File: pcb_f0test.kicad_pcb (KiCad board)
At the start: 2 copper layers, 50 x 6 mm, 36 parts, among them P1 CONN_02X04, P2 CONN_01X02, U1 STM32F042GxU, U2 LP2985LV

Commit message: Fairly good routing now.
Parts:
- moved C2 0.20 mm to (43.1, 63.2)
- moved C4 0.20 mm to (44.1, 63.2)
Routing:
- net /boot0: track 21.3 -> 25.5 mm
- net /ldr6: track 32.0 -> 31.1 mm
- net /ldb1: track 32.8 -> 32.0 mm
- net /ldr2: track 13.3 -> 14.0 mm
- net /ldr5: track 28.5 -> 27.8 mm
- net +3V3: track 56.4 -> 55.8 mm
- added copper zone on B.Cu, net +3V3

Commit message: Some misc. changes.
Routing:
- added copper zone on F.Cu, net +3V3
- added copper zone on B.Cu, net GND
- added copper zone on F.Cu, net GND

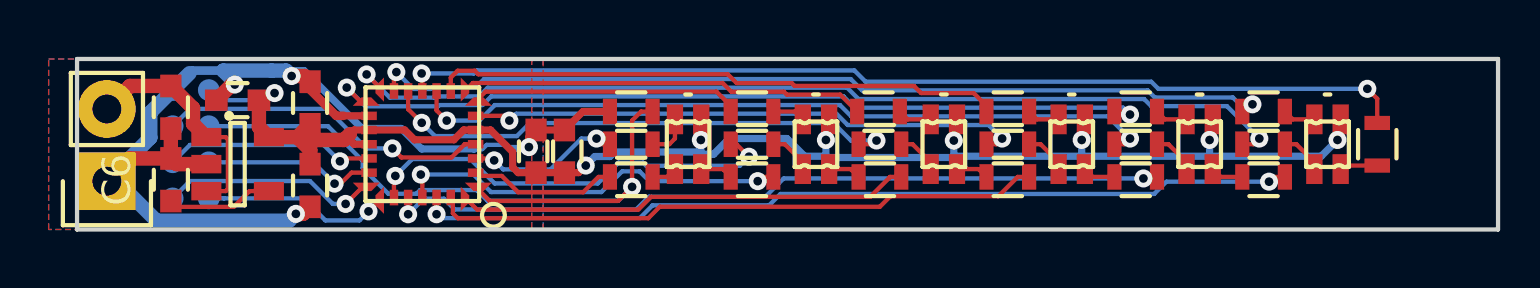
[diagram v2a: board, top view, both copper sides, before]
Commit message: Fix corner pads on QFN.
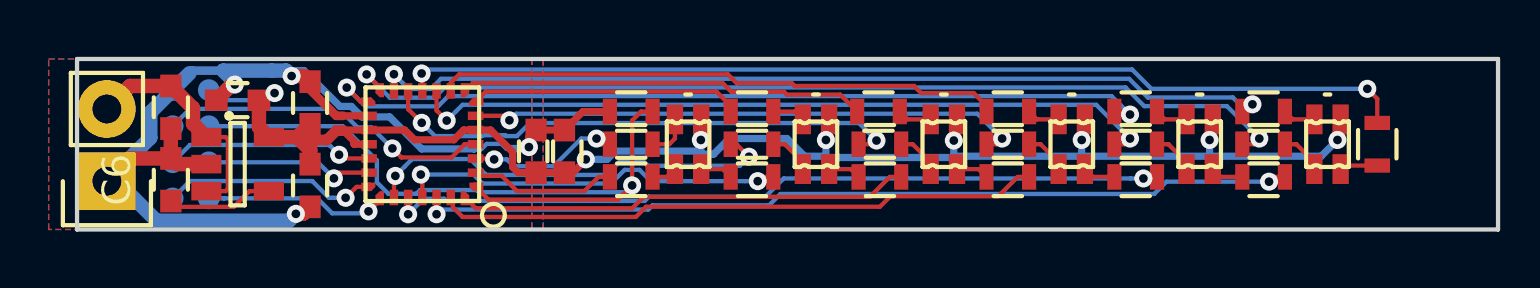
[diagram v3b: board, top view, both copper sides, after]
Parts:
- U1: footprint knielsenlib:UFQFPN28 -> knielsenlib:UFQFPN28_fixpad

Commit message: Fix numbering of LEDs.
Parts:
- renumbered LD2 to LD1, LD3 to LD2, LD4 to LD3, LD5 to LD4, LD6 to LD5, LD1 to LD6
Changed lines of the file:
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@@
     (at 71 63 90)
     (descr "RGB led, 0603")
-    (fp_text reference LD1 (at 0 -1.15 90) (layer F.SilkS) hide
+    (fp_text reference LD6 (at 0 -1.15 90) (layer F.SilkS) hide
       (effects (font (size 0.20066 0.20066) (thickness 0.04064)))
     )
@@
     (at 48.5 63 90)
     (descr "RGB led, 0603")
-    (fp_text reference LD2 (at 0 -1.15 90) (layer F.SilkS) hide
+    (fp_text reference LD1 (at 0 -1.15 90) (layer F.SilkS) hide
       (effects (font (size 0.20066 0.20066) (thickness 0.04064)))
     )
@@
     (at 53 63 90)
     (descr "RGB led, 0603")
-    (fp_text reference LD3 (at 0 -1.15 90) (layer F.SilkS) hide
+    (fp_text reference LD2 (at 0 -1.15 90) (layer F.SilkS) hide
       (effects (font (size 0.20066 0.20066) (thickness 0.04064)))
     )
@@
     (at 57.5 63 90)
     (descr "RGB led, 0603")
-    (fp_text reference LD4 (at 0 -1.15 90) (layer F.SilkS) hide
+    (fp_text reference LD3 (at 0 -1.15 90) (layer F.SilkS) hide
       (effects (font (size 0.20066 0.20066) (thickness 0.04064)))
     )
@@
     (at 62 63 90)
     (descr "RGB led, 0603")
-    (fp_text reference LD5 (at 0 -1.15 90) (layer F.SilkS) hide
+    (fp_text reference LD4 (at 0 -1.15 90) (layer F.SilkS) hide
       (effects (font (size 0.20066 0.20066) (thickness 0.04064)))
     )
@@
     (at 66.5 63 90)
     (descr "RGB led, 0603")
-    (fp_text reference LD6 (at 0 -1.15 90) (layer F.SilkS) hide
+    (fp_text reference LD5 (at 0 -1.15 90) (layer F.SilkS) hide
       (effects (font (size 0.20066 0.20066) (thickness 0.04064)))
     )

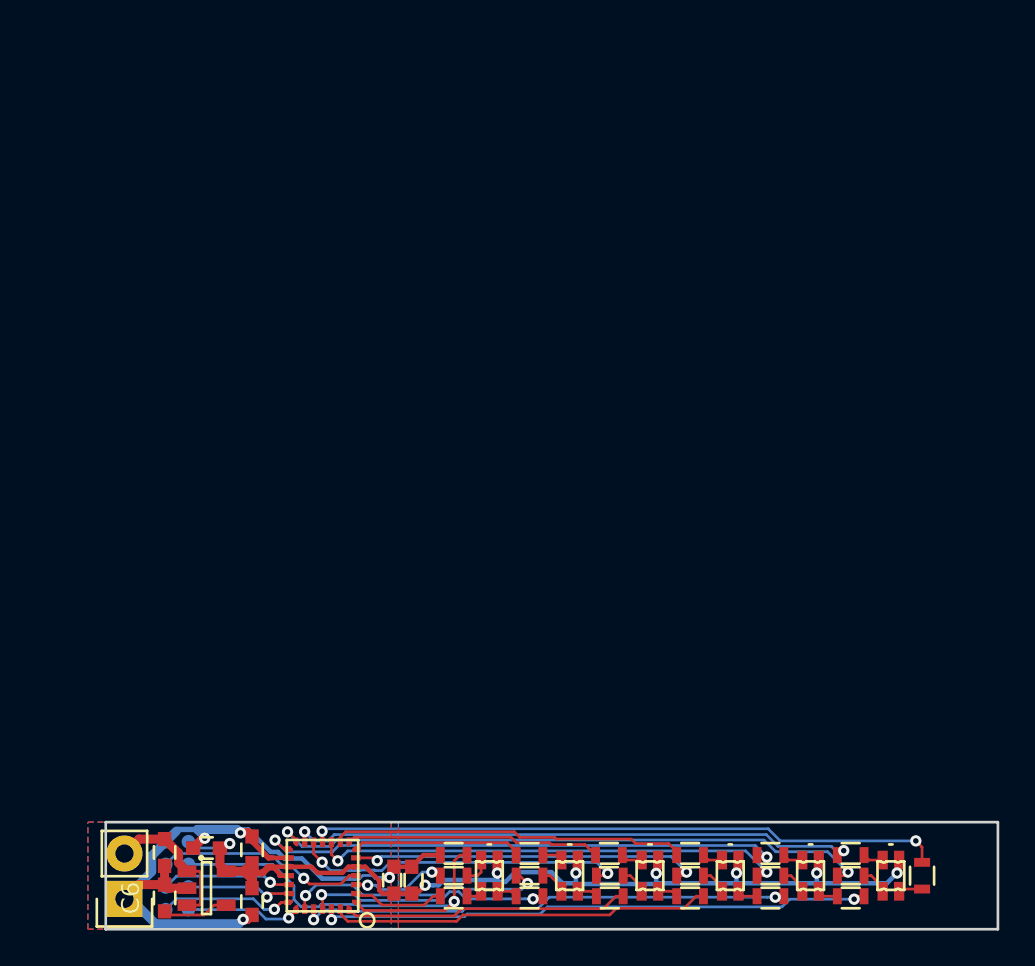
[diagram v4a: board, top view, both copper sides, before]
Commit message: Add pogopin board, fixing pogopad layout.
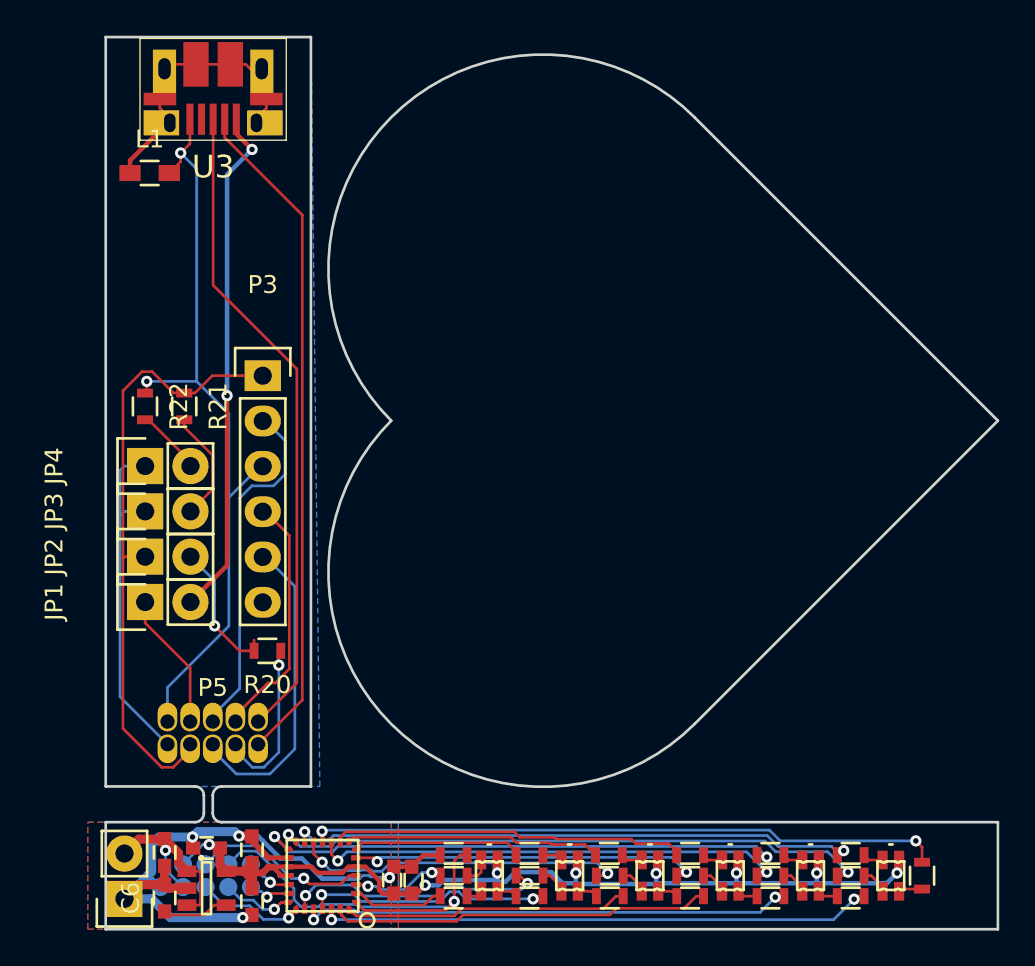
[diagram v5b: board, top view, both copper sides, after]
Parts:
- removed P1: CONN_02X04, knielsenlib:TestPoints2x4
- added JP1: Jumper_NC_Small, Pin_Headers:Pin_Header_Straight_1x02, F.Cu at (29.2, 47.7)
- added JP2: Jumper_NC_Small, Pin_Headers:Pin_Header_Straight_1x02, F.Cu at (29.2, 45.1)
- added JP3: Jumper_NC_Small, Pin_Headers:Pin_Header_Straight_1x02, F.Cu at (29.2, 42.6)
- added JP4: Jumper_NC_Small, Pin_Headers:Pin_Header_Straight_1x02, F.Cu at (29.2, 40.0)
- added L1: ferrite, Resistors_SMD:R_0603_HandSoldering, F.Cu at (29.5, 23.6)
- added P3: CONN_01X06, Pin_Headers:Pin_Header_Straight_1x06, F.Cu at (35.8, 35.0)
- added P5: CONN_02X05, knielsenlib:pogopins_2x5_50mil, F.Cu at (33.0, 55.0)
- added P6: CONN_02X05, knielsenlib:pogopads_2x5_50mil_smd, B.Cu at (32.6, 63.0)
- added R20: 510, Resistors_SMD:R_0603, F.Cu at (36.1, 50.4)
- added R21: 510, Resistors_SMD:R_0603, F.Cu at (31.4, 36.7)
- added R22: 510, Resistors_SMD:R_0603, F.Cu at (29.2, 36.7)
- added U3: KNUSB, knielsenlib:10103594-0001LF, F.Cu at (33.0, 17.8)
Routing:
- net /sheet_pogopins/pogo_gnd: track 0.00 -> 44.0 mm, vias 0 -> 2
- net /sheet_pogopins/pogo_dm: track 0.00 -> 37.9 mm
- net /sheet_pogopins/pogo_dp: track 0.00 -> 36.6 mm
- net /sheet_pogopins/tg_pwr: track 0.00 -> 34.8 mm
- net /sheet_pogopins/usb_vbus: track 0.00 -> 28.9 mm, vias 0 -> 2
- net /sheet_pogopins/tg_swclk: track 0.00 -> 19.8 mm
- net Net-(JP3-Pad1): track 0.00 -> 19.5 mm
- net /sheet_pogopins/tg_nrst: track 0.00 -> 17.7 mm
- net Net-(L1-Pad1): track 0.00 -> 16.2 mm
- net /sheet_pogopins/tg_swdio: track 0.00 -> 14.0 mm
- net /sheet_pogopins/pogo_boot0: track 0.00 -> 9.24 mm, vias 0 -> 1
- net Net-(JP2-Pad2): track 0.00 -> 7.83 mm, vias 0 -> 1
- net /sheet_pogopins/pogo_vbus: track 0.00 -> 7.74 mm
- net Net-(JP3-Pad2): track 0.00 -> 6.31 mm
- net /usb_dm: track 7.36 -> 2.64 mm
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- added copper zone on B.Cu, net /sheet_pogopins/pogo_gnd
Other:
- board size 50 x 6 mm -> 50 x 50 mm

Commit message: Initial stab at a "christmas heart" decoration pcb.
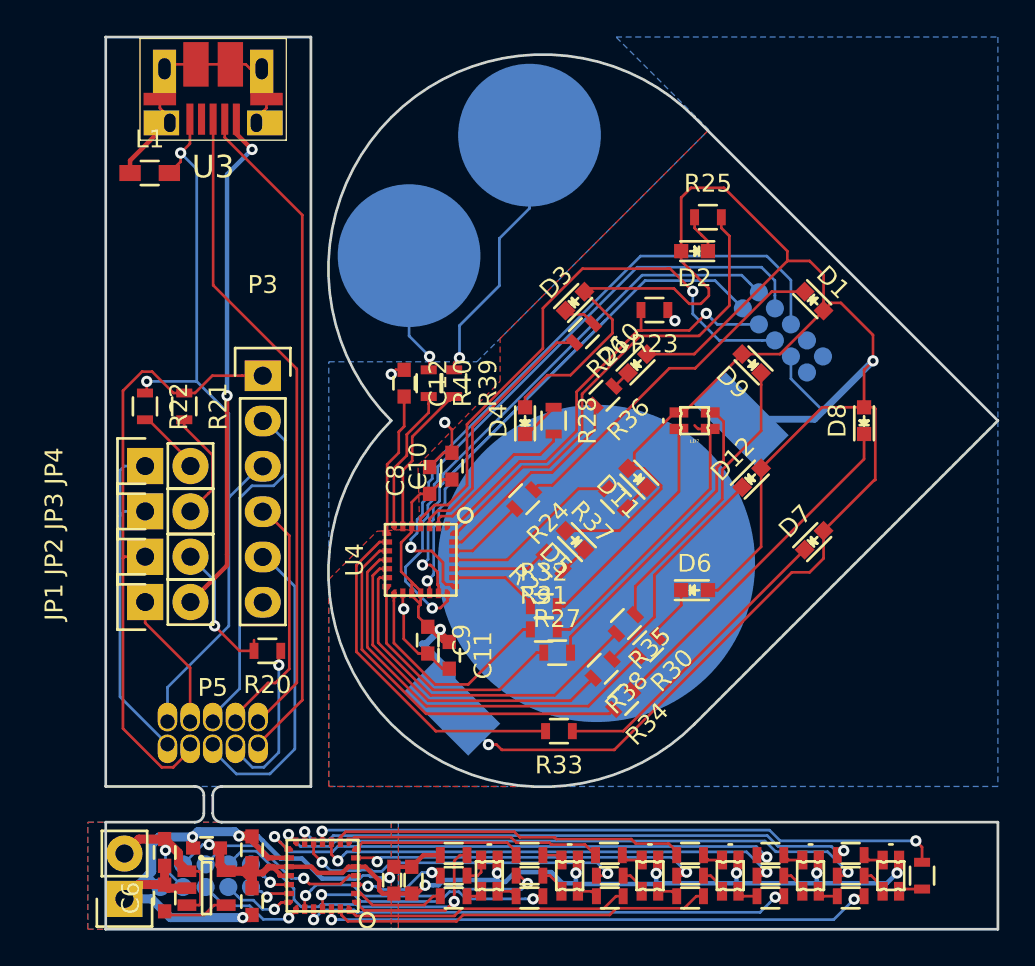
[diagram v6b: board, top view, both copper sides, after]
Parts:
- added BT1: Battery, knielsenlib:Linx_BAT_HLD_001, B.Cu at (54.5, 45.5)
- added C10: 4.7u, Capacitors_SMD:C_0603, F.Cu at (46.4, 40.0)
- added C11: 4.7u, Capacitors_SMD:C_0603, F.Cu at (46.2, 50.6)
- added C12: 47n, Capacitors_SMD:C_0603, F.Cu at (43.7, 35.4)
- added C8: 100n, Capacitors_SMD:C_0603, F.Cu at (45.1, 40.9)
- added C9: 100n, Capacitors_SMD:C_0603, F.Cu at (45.0, 49.8)
- added D1: Led_Small, LEDs:LED_0603, F.Cu at (66.7, 30.8)
- added D10: Led_Small, LEDs:LED_0603, F.Cu at (56.8, 34.3)
- added D11: Led_Small, LEDs:LED_0603, F.Cu at (56.8, 40.7)
- added D12: Led_Small, LEDs:LED_0603, F.Cu at (63.2, 40.7)
- added D2: Led_Small, LEDs:LED_0603, F.Cu at (60.0, 28.0)
- added D3: Led_Small, LEDs:LED_0603, F.Cu at (53.3, 30.8)
- added D4: Led_Small, LEDs:LED_0603, F.Cu at (50.5, 37.5)
- added D5: Led_Small, LEDs:LED_0603, F.Cu at (53.3, 44.2)
- added D6: Led_Small, LEDs:LED_0603, F.Cu at (60.0, 47.0)
- added D7: Led_Small, LEDs:LED_0603, F.Cu at (66.7, 44.2)
- added D8: Led_Small, LEDs:LED_0603, F.Cu at (69.5, 37.5)
- added D9: Led_Small, LEDs:LED_0603, F.Cu at (63.2, 34.3)
- added LD7: RGB, knielsenlib:RGB_0603, F.Cu at (60.0, 37.5)
- added P1: CONN_02X05, knielsenlib:pogopads_2x5_50mil_smd, B.Cu at (65.0, 32.6)
- added P7: CONN_01X01, knielsenlib:Touchpad_8mm, B.Cu at (50.8, 21.5)
- added P8: CONN_01X01, knielsenlib:Touchpad_8mm, B.Cu at (44.0, 28.2)
- added R23: 47k, Resistors_SMD:R_0603, F.Cu at (57.8, 31.3)
- added R24: 560, Resistors_SMD:R_0603, F.Cu at (50.5, 41.9)
- added R25: 560, Resistors_SMD:R_0603, F.Cu at (60.8, 26.1)
- added R26: 560, Resistors_SMD:R_0603, F.Cu at (53.8, 32.6)
- added R27: 560, Resistors_SMD:R_0603, F.Cu at (52.3, 50.5)
- added R28: 560, Resistors_SMD:R_0603, F.Cu at (52.1, 37.5)
- added R29: 560, Resistors_SMD:R_0603, F.Cu at (52.1, 45.4)
- added R30: 560, Resistors_SMD:R_0603, F.Cu at (57.4, 50.1)
- added R31: 100, Resistors_SMD:R_0603, F.Cu at (51.5, 49.2)
- added R32: 100, Resistors_SMD:R_0603, F.Cu at (51.5, 47.9)
- added R33: 560, Resistors_SMD:R_0603, F.Cu at (52.4, 54.9)
- added R34: 560, Resistors_SMD:R_0603, F.Cu at (56.0, 53.1)
- added R35: 560, Resistors_SMD:R_0603, F.Cu at (56.1, 48.9)
- added R36: 560, Resistors_SMD:R_0603, F.Cu at (55.0, 36.1)
- added R37: 560, Resistors_SMD:R_0603, F.Cu at (55.6, 41.9)
- added R38: 560, Resistors_SMD:R_0603, F.Cu at (54.9, 51.4)
- added R39: 10k, Resistors_SMD:R_0603, F.Cu at (46.5, 35.4)
- added R40: 10k, Resistors_SMD:R_0603, F.Cu at (45.1, 35.4)
- added U4: STM32F042GxU, knielsenlib:UFQFPN28_fixpad, F.Cu at (44.6, 45.3)
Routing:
- net +3V3: track 55.5 -> 219.1 mm, vias 8 -> 11
- net /sheet_heart/h_usb_dm: track 0.00 -> 41.1 mm, vias 0 -> 1
- net /sheet_heart/h_swclk: track 0.00 -> 37.0 mm, vias 0 -> 1
- net /sheet_heart/h_swdio: track 0.00 -> 36.0 mm, vias 0 -> 1
- net /sheet_heart/h_nrst: track 0.00 -> 31.8 mm, vias 0 -> 1
- net /sheet_heart/h_usb_dp: track 0.00 -> 30.5 mm, vias 0 -> 1
- net /sheet_heart/h_ld5: track 0.00 -> 27.0 mm
- net /sheet_heart/h_boot0: track 0.00 -> 25.0 mm, vias 0 -> 1
- net /sheet_heart/h_ld10: track 0.00 -> 23.4 mm
- net /sheet_heart/h_ld7: track 0.00 -> 22.1 mm
- net /sheet_heart/h_ld11: track 0.00 -> 20.1 mm
- net /sheet_heart/h_ild1: track 0.00 -> 19.8 mm
- net /sheet_heart/h_ild7: track 0.00 -> 19.7 mm
- net /sheet_heart/h_ld3: track 0.00 -> 19.6 mm
- net /sheet_heart/h_ld12: track 0.00 -> 19.0 mm
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- added copper zone on B.Cu, net GNDD
